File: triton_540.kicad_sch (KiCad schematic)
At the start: 41 parts, among them J1 REC ANT, J3 Conn_01x04, J4 AUX 12V, J5 KEY, J6 PTT, Y1 13.99MHz, Y2 14.49MHz, Y3 14.99MHz, Y4 15.49MHz

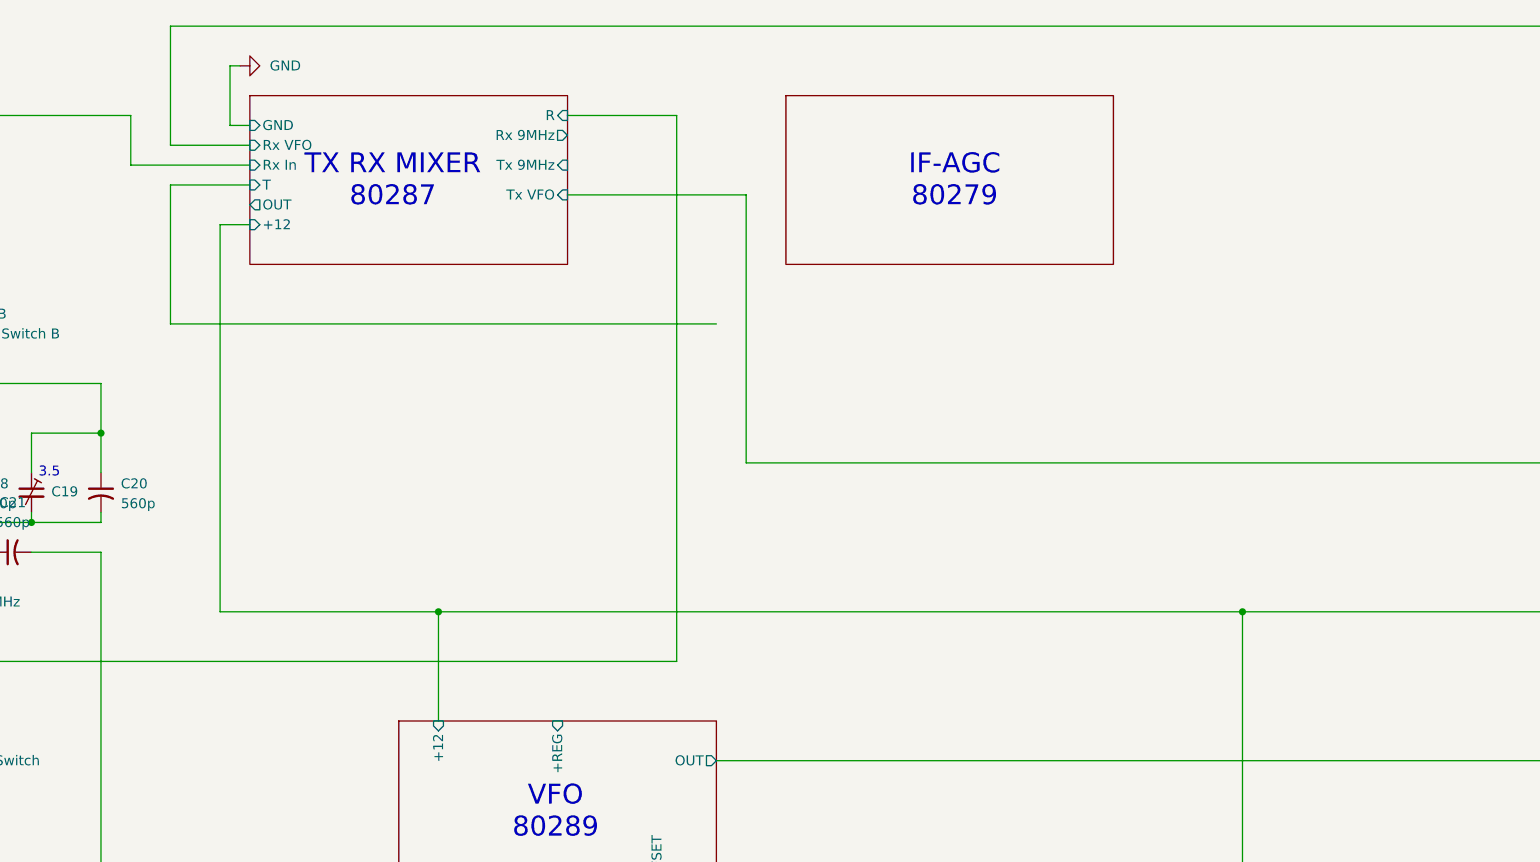
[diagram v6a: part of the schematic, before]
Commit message: sims 1-3 run on ig-agc
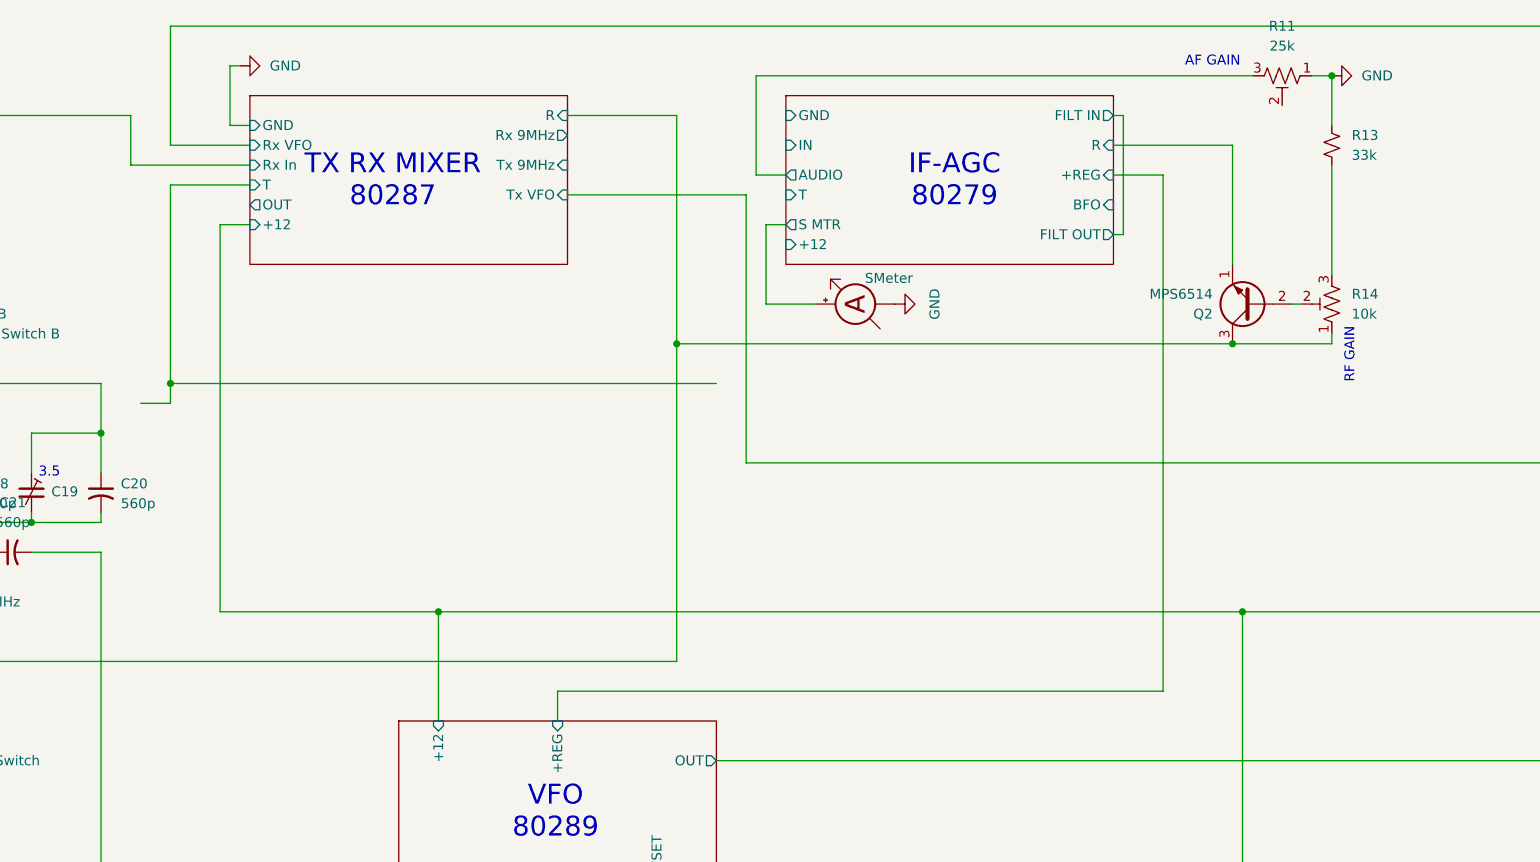
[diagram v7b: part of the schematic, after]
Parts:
- added MES1: SMeter, symbol Device:Ammeter_DC
- added Q2: MPS6514, symbol Transistor_BJT:Q_NPN_EBC
- added R11: 25k, symbol Device:R_Potentiometer_Trim_US
- added R13: 33k, symbol Device:R_Small_US
- added R14: 10k, symbol Device:R_Potentiometer_Trim_US
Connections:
- net GND: now also MES1.1 (-), R11.1, R13.1
- net RF_Amp_80166/R: now also Q2.3 (C), R14.1
- new net: Q2.2 (B), R14.2
- new net: R13.2, R14.3
- new net IF-AGC_80279/AUDIO: R11.3
- new net IF-AGC_80279/R: Q2.1 (E)
- new net IF-AGC_80279/S MTR: MES1.2 (+)
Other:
- sheet IF-AGC_80279 ports: added +12, +REG, AUDIO, BFO, FILT IN, FILT OUT, GND, IN, R, S MTR, T; removed none
- note added: "AF GAIN"
- note added: "RF GAIN"
